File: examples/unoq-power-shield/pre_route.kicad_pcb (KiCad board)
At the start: 4 copper layers, 53.3 x 68.6 mm, 56 parts, among them J1 VIN 7-24V, J10 UNO PWR, J11 UNO ANALOG, J12 UNO D0-D7, J13 UNO D8-SCL, J2 5V OUT, J3 Qwiic, J4 Qwiic, J5 5V IO, Q1 BSS138LT1G, Q2 BSS138LT1G, Q3 BSS138LT1G, Q4 BSS138LT1G, Q5 AO4407A, U1 TPS54331DDAR, U2 INA226AIDGSR

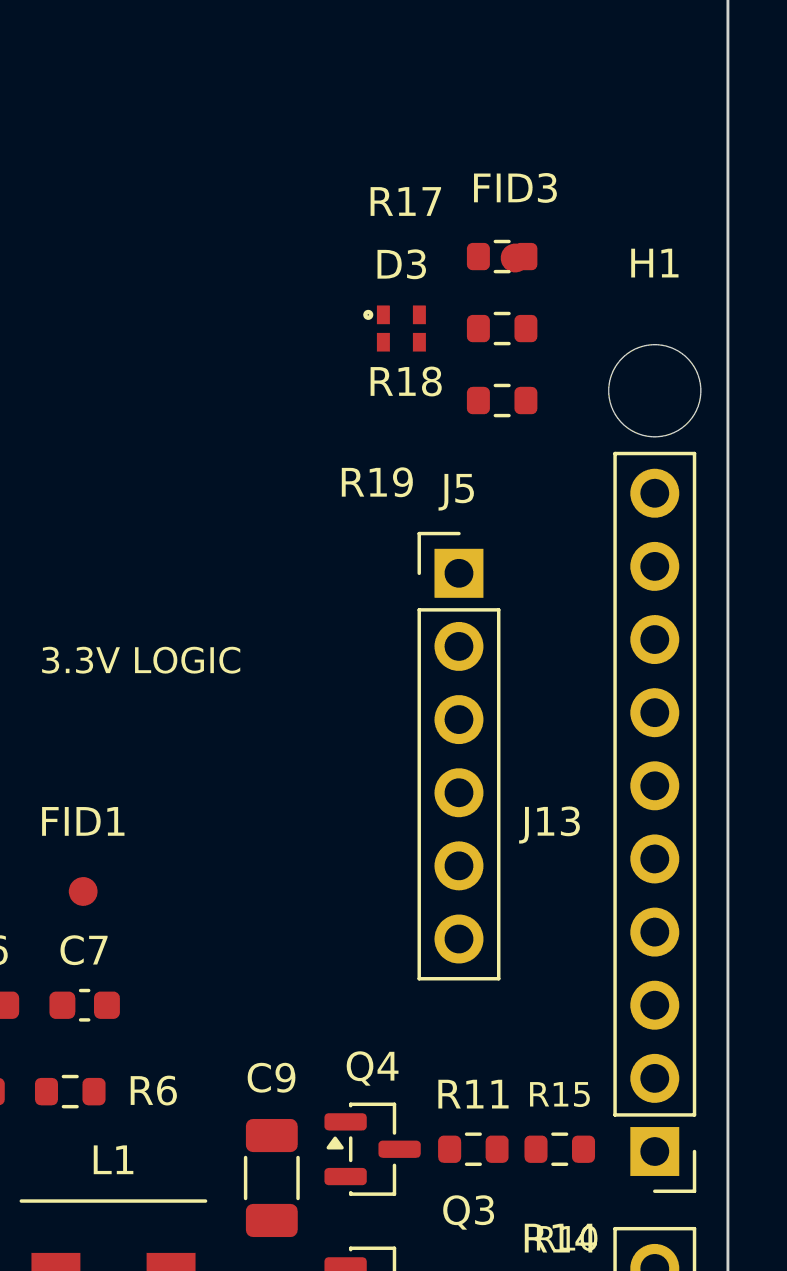
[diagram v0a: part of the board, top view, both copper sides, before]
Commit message: Routing loop closed: xvfb in route.py, DSN sanity, checker interior test
Four measured fixes from driving the example board through route/check:

- route.py wraps freerouting 1.9.0 in xvfb-run when headless (the Xvfb
  decision lived only in the Dockerfile; the invocation still died with
  HeadlessException).
- export_dsn withholds SURFACE pours from the DSN (in-memory only):
  ExportSpecctraDSN writes every zone as a Specctra (plane ...) that
  freerouting treats as fixed copper, so a ground flood on a routable
  layer walls off the whole layer - measured 16 unfinished nets on a
  2-signal-layer board. Plane-layer pours stay: that IS the semantics.
  It also sanitises class names: KiCad 10 exports "Power,Default" and
  the comma splits the Specctra token, so freerouting never bound those
  nets and routed power at the default width - the exact thin-power
  failure the checker flagged.
- validate_gerbers keepout test uses the strict interior (1um epsilon):
  a pour correctly carved around a keepout leaves vertices exactly ON
  the boundary, and flagging those fails every fill that did the right
  thing.
- zones.py fills to a temp file and swaps (kct now refuses -o == input),
  and its fill verification runs in a fresh interpreter (second
  LoadBoard after zone edits returns a bare SwigPyObject).

Example board across these rounds: checker 12->13 passed, antenna
keepout PASS with real carved pours, VIN/VIN_PROT/VIN_RAW at 0.30, DRC
unconnected 6 -> 2, violation kinds stable across all 5 samples.

Co-Authored-By: Claude Fable 5 <noreply@anthropic.com>
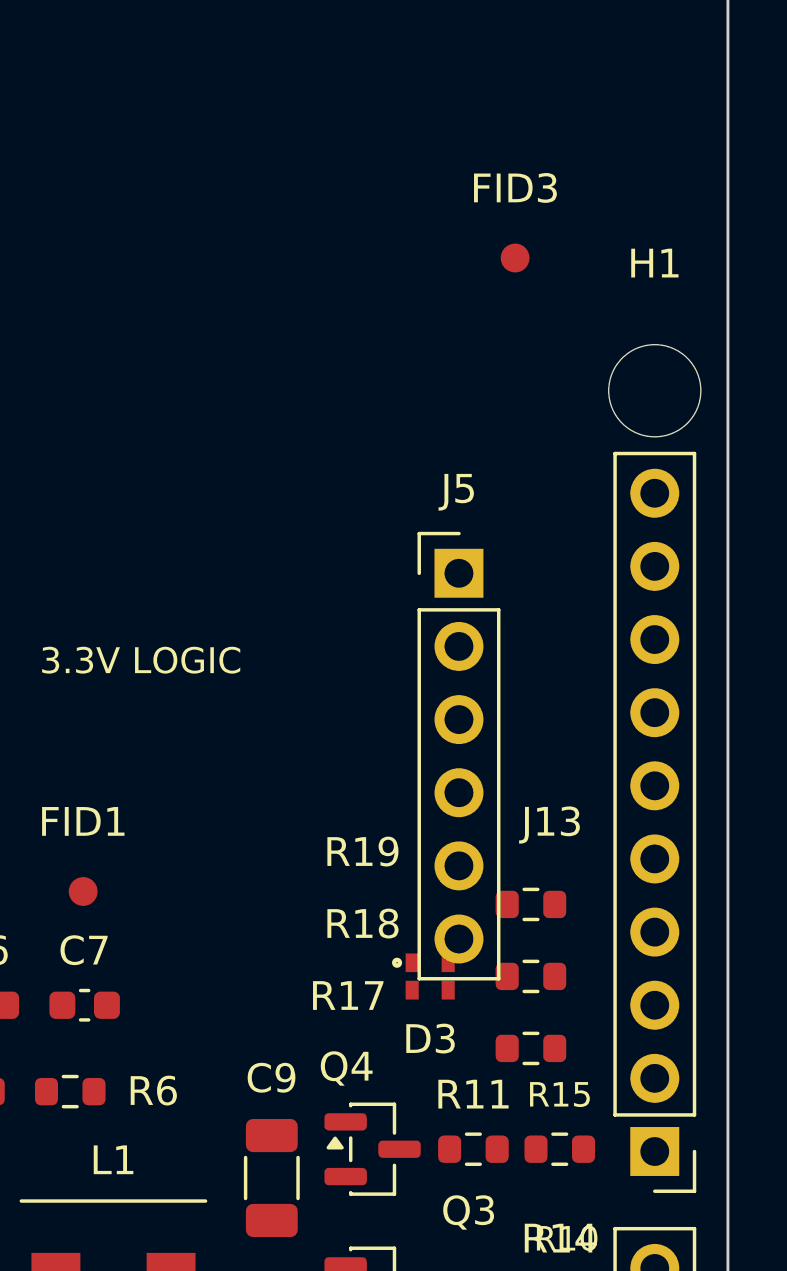
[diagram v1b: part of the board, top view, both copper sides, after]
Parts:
- moved R17 27.5 mm to (168.3, 108.8)
- moved D3 22.5 mm to (164.8, 106.3)
- moved R18 22.5 mm to (168.3, 106.3)
- moved R19 17.5 mm to (168.3, 103.8)

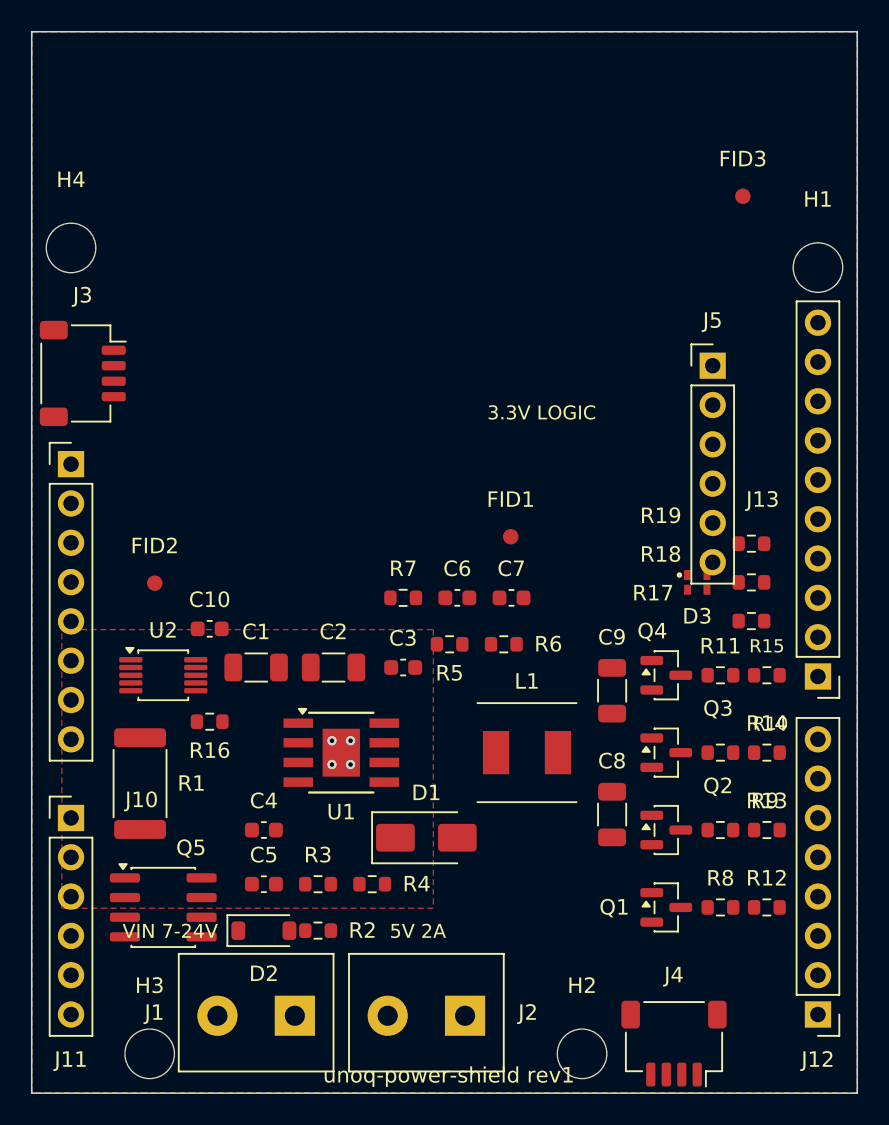
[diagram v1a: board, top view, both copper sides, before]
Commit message: Example board: gerber checker green (14/0); idempotency proven byte-for-byte
Round 4: J5 moved off D3 (its pins run DOWNWARD from pin1 - pin 6 landed
on the LED and shorted RGB_G to GND), netclass clearance aligned to
KiCad's 0.2 DRC default end to end (freerouting was routing to the
bootstrapped 0.15 and every squeeze became a DRC violation), a real
VIN_RAW pour over the 4 A entry corridor, GND stitching vias on the
Qwiic mounting tabs.

The checker now passes the board's own export: 14 passed / 2 not checked
/ 0 failed, with plane_fed exempting exactly the 9 measured pad-escape
stubs (15.6 mm, all chains <= 3 mm). Run-twice-diff idempotency:
generate_schematic, floorplan and add_mounting_holes are byte-identical
on the second run.

Still open before this board is orderable (the plan's gate list holds
it): 9 clearance squeezes in the buck cluster (completion passes use
their own 0.16 defaults - set [route.completion] clearance next), a 2 mm
5V hop at D3, one GND island wanting a stitch. DRC is stable across all
5 samples; no unstable kinds.

Co-Authored-By: Claude Fable 5 <noreply@anthropic.com>
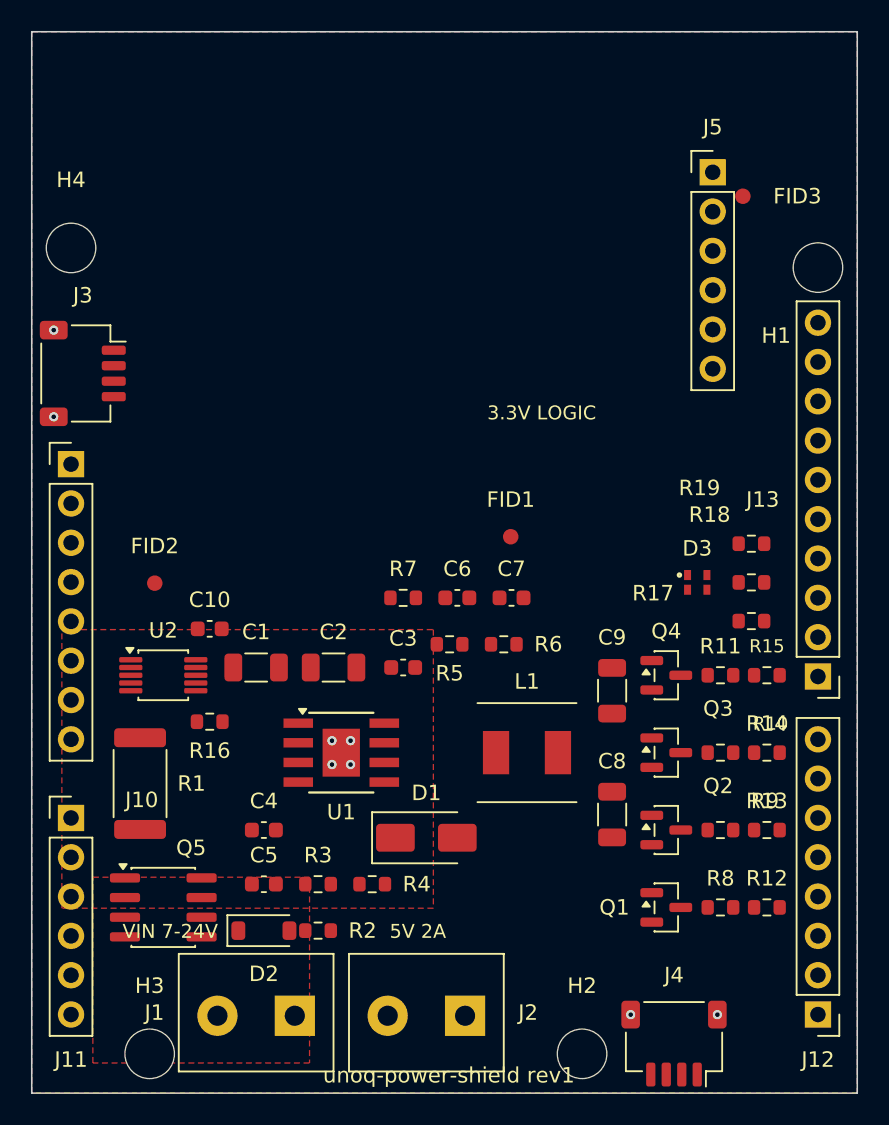
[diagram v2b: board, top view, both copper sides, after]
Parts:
- moved J5 12.5 mm to (165.8, 79.8)
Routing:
- net GND: vias 4 -> 8
- added copper zone on F.Cu, net VIN_RAW
